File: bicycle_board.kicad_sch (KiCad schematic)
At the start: 59 parts, among them J1 Micro_SD_Card, J10 USB_A, J12 Conn_01x04, J13 Conn_01x04, J2 USB_C_Receptacle_USB2.0_16P, J6 Conn_01x08, J7 Conn_01x05, J8 Conn_01x02, J9 Conn_01x06, Q1 Q_NMOS_GSD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

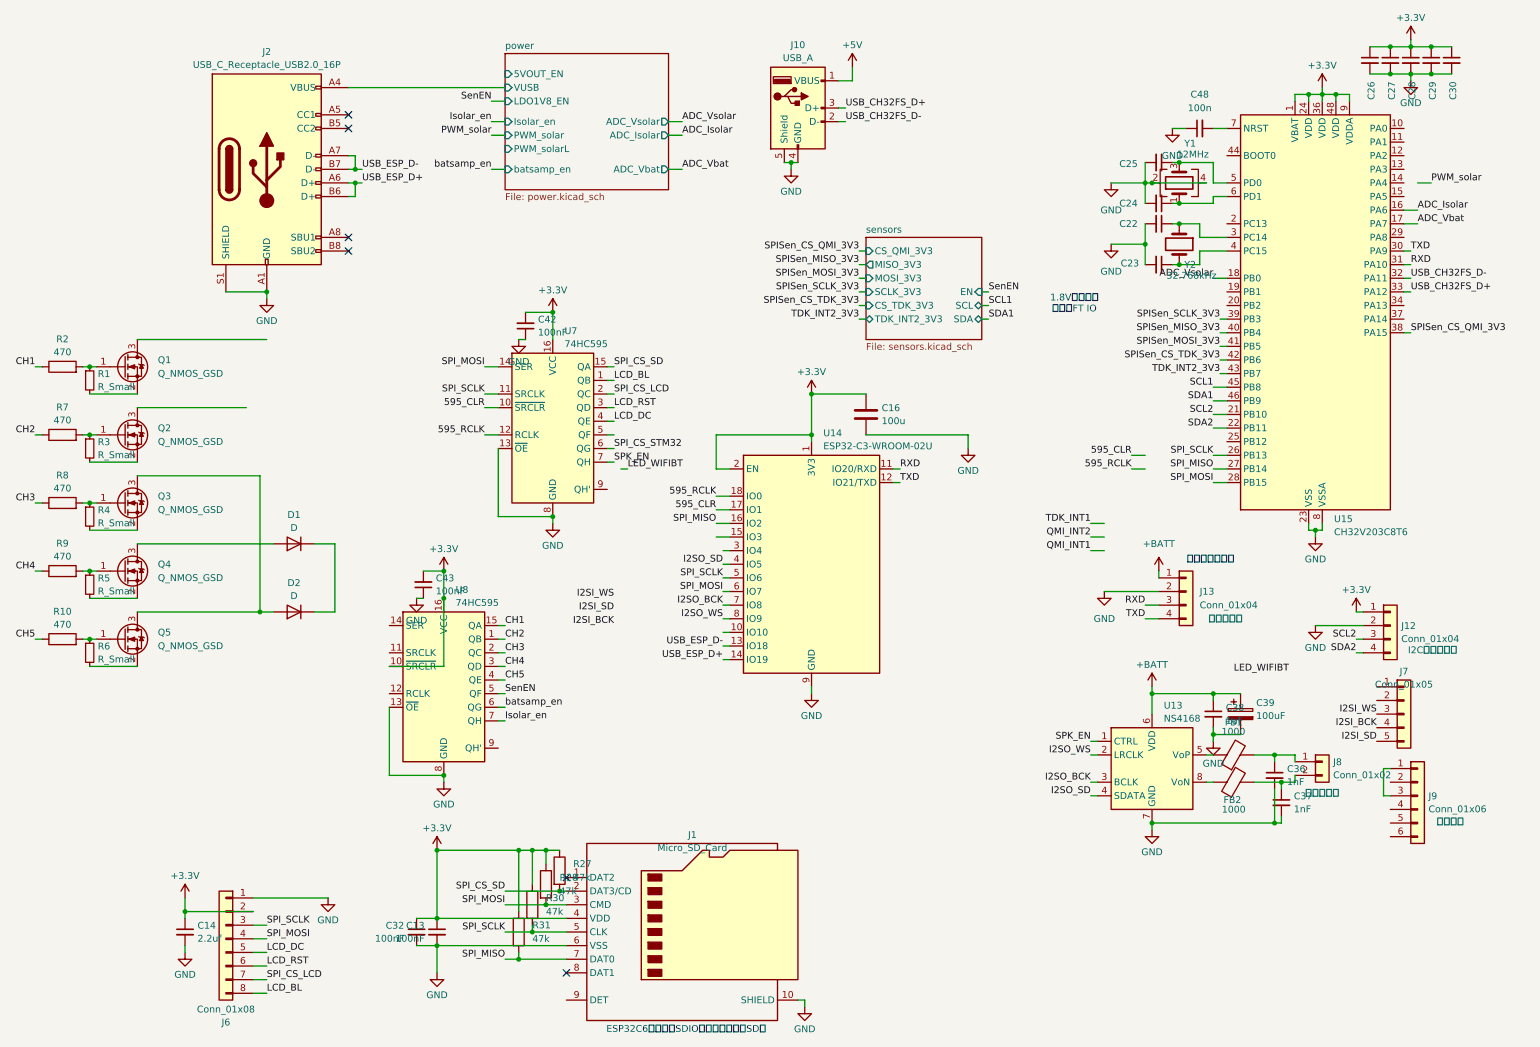
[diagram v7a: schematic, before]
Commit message: 移除第二个74HC595，SGM2033-1.8改成一直开启，按PCA9306数据手册修改供电
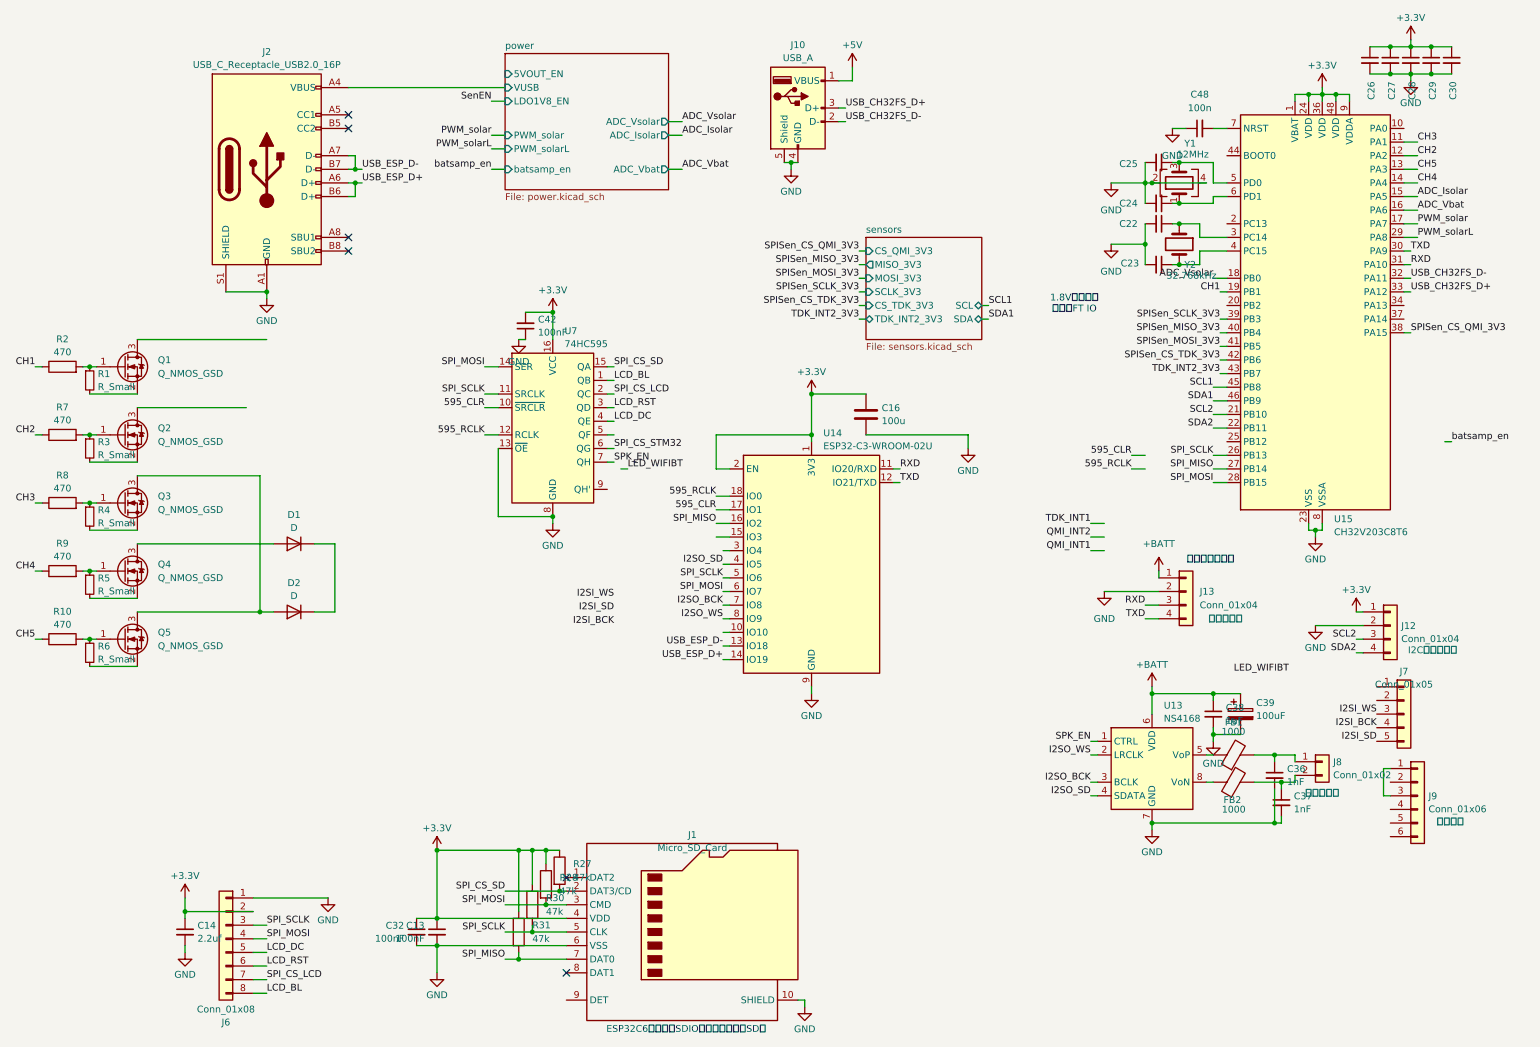
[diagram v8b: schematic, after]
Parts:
- removed C43: 100nF, Capacitor_SMD:C_0402_1005Metric, symbol Device:C_Small
- removed U8: 74HC595, Package_SO:SSOP-16_4.4x5.2mm_P0.65mm, symbol 74xx:74HC595
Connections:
- net ADC_Isolar: now also U15.15 (PA5); no longer U15.16 (PA6)
- net ADC_Vbat: now also U15.16 (PA6); no longer U15.17 (PA7)
- net CH1: now also U15.19 (PB1)
- net CH2: now also U15.12 (PA2)
- net CH3: now also U15.11 (PA1)
- net CH4: now also U15.14 (PA4)
- net CH5: now also U15.13 (PA3)
- net PWM_solar: now also U15.17 (PA7)
- net PWM_solarL: now reaches U15.29 (PA8)
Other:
- sheet power ports: added none; removed Isolar_en
- sheet sensors ports: added none; removed EN
